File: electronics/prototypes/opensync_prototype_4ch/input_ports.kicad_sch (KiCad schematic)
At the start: 5 parts, among them J2 61611042121502, U4 SN74LVC1G17DCKR

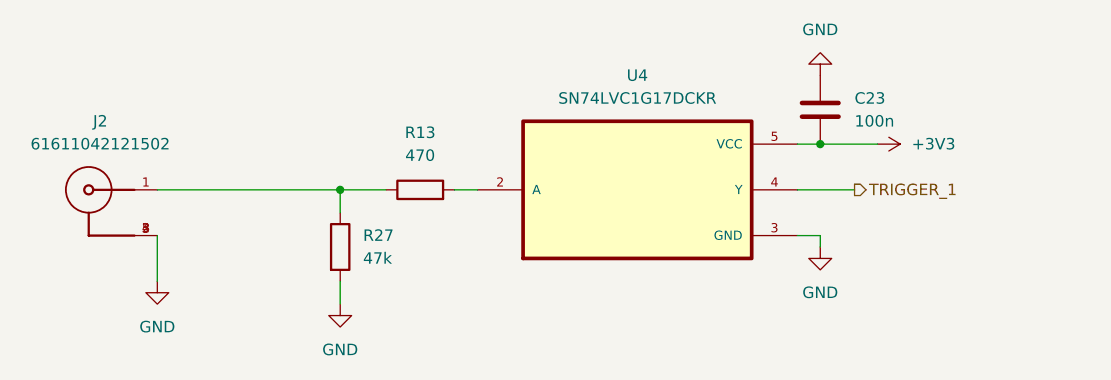
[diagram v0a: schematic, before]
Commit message: Added part numbers
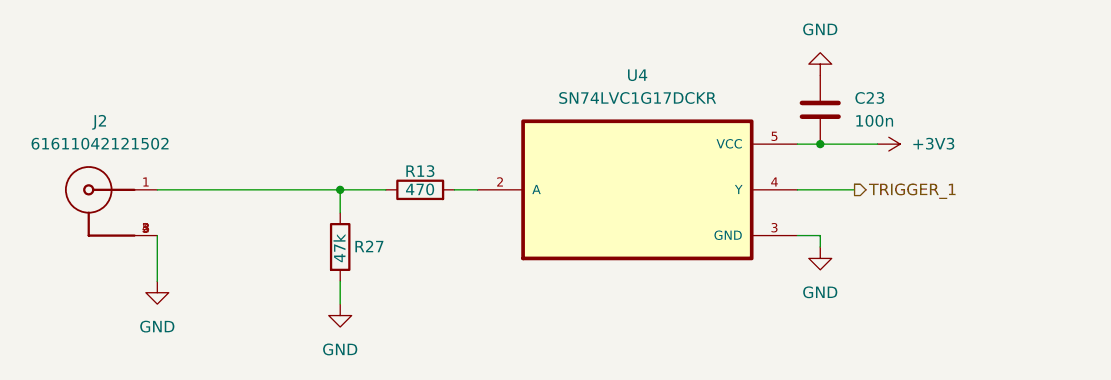
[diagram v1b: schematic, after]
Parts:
- C23: LCSC (none) -> C60474
- R13: LCSC (none) -> C482182
- R27: LCSC (none) -> C176117
- U4: LCSC (none) -> C10425
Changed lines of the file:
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@@
+			)
+		)
+		(property "LCSC" "C10425"
+			(at 138.43 66.04 0)
+			(effects
+				(font
+					(size 1.27 1.27)
+				)
+				(hide yes)
 			)
 		)
@@
 		(on_board yes)
 		(dnp no)
-		(fields_autoplaced yes)
 		(property "Reference" "R27"
-			(at 107.95 71.1199 0)
+			(at 106.934 72.39 0)
 			(effects
 				(font
@@
 		)
 		(property "Value" "47k"
-			(at 107.95 73.6599 0)
+			(at 105.41 74.168 90)
 			(effects
 				(font
@@
 			)
 		)
+		(property "LCSC" "C176117"
+			(at 105.41 72.39 0)
+			(effects
+				(font
+					(size 1.27 1.27)
+				)
+				(hide yes)
+			)
+		)
 		(pin "2"
 		)
@@
 		(on_board yes)
 		(dnp no)
-		(fields_autoplaced yes)
 		(property "Reference" "R13"
-			(at 114.3 59.69 90)
+			(at 114.3 64.008 90)
 			(effects
 				(font
@@
 		)
 		(property "Value" "470"
-			(at 114.3 62.23 90)
+			(at 114.3 66.04 90)
 			(effects
 				(font
@@
 		)
 		(property "Description" "Resistor"
+			(at 114.3 66.04 0)
+			(effects
+				(font
+					(size 1.27 1.27)
+				)
+				(hide yes)
+			)
+		)
+		(property "LCSC" "C482182"
 			(at 114.3 66.04 0)
 			(effects
@@
 			)
 		)
+		(property "LCSC" ""
+			(at 77.47 66.04 0)
+			(effects
+				(font
+					(size 1.27 1.27)
+				)
+			)
+		)
 		(pin "4"
 		)
@@
 			(at 158.75 57.15 0)
 			(effects
+				(font
+					(size 1.27 1.27)
+				)
+				(hide yes)
+			)
+		)
+		(property "LCSC" "C60474"
+			(at 158.75 57.15 0)
+			(effects

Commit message: More prototyping
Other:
- moved on the sheet: C23
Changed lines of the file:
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@@
-	)
-	(junction
-		(at 158.75 60.96)
-		(diameter 0)
-		(color 0 0 0 0)
 	)
 	(junction
@@
 		(color 0 0 0 0)
 	)
+	(junction
+		(at 171.45 60.96)
+		(diameter 0)
+		(color 0 0 0 0)
+	)
 	(wire
 		(pts
@@
 	(wire
 		(pts
-			(xy 156.21 60.96) (xy 158.75 60.96)
+			(xy 171.45 60.96) (xy 186.69 60.96)
+		)
+		(stroke
+			(width 0)
+			(type default)
+		)
+	)
+	(wire
+		(pts
+			(xy 156.21 60.96) (xy 171.45 60.96)
 		)
 		(stroke
@@
 	(wire
 		(pts
+			(xy 171.45 57.15) (xy 171.45 60.96)
+		)
+		(stroke
+			(width 0)
+			(type default)
+		)
+	)
+	(wire
+		(pts
 			(xy 110.49 66.04) (xy 105.41 66.04)
 		)
@@
 		(pts
 			(xy 105.41 66.04) (xy 105.41 68.58)
-		)
-		(stroke
-			(width 0)
-			(type default)
-		)
-	)
-	(wire
-		(pts
-			(xy 158.75 60.96) (xy 165.1 60.96)
 		)
 		(stroke
@@
 	(symbol
 		(lib_id "power:GND")
-		(at 158.75 53.34 180)
+		(at 186.69 68.58 0)
 		(unit 1)
 		(exclude_from_sim no)
@@
 		(fields_autoplaced yes)
 		(property "Reference" "#PWR014"
-			(at 158.75 46.99 0)
+			(at 186.69 74.93 0)
 			(effects
 				(font
@@
 		)
 		(property "Value" "GND"
-			(at 158.75 48.26 0)
+			(at 186.69 73.66 0)
 			(effects
 				(font
@@
 		)
 		(property "Footprint" ""
-			(at 158.75 53.34 0)
+			(at 186.69 68.58 0)
 			(effects
 				(font
@@
 		)
 		(property "Datasheet" ""
-			(at 158.75 53.34 0)
+			(at 186.69 68.58 0)
 			(effects
 				(font
@@
 		)
 		(property "Description" "Power symbol creates a global label with name \"GND\" , ground"
-			(at 158.75 53.34 0)
+			(at 186.69 68.58 0)
 			(effects
 				(font
@@
 	(symbol
 		(lib_id "power:+3V3")
-		(at 165.1 60.96 270)
+		(at 171.45 57.15 0)
 		(unit 1)
 		(exclude_from_sim no)
@@
 		(fields_autoplaced yes)
 		(property "Reference" "#PWR013"
-			(at 161.29 60.96 0)
+			(at 171.45 60.96 0)
 			(effects
 				(font
@@
 		)
 		(property "Value" "+3V3"
-			(at 168.91 60.9599 90)
-			(effects
-				(font
-					(size 1.27 1.27)
-				)
-				(justify left)
+			(at 171.45 52.07 0)
+			(effects
+				(font
+					(size 1.27 1.27)
+				)
 			)
 		)
 		(property "Footprint" ""
-			(at 165.1 60.96 0)
+			(at 171.45 57.15 0)
 			(effects
 				(font
@@
 		)
 		(property "Datasheet" ""
-			(at 165.1 60.96 0)
+			(at 171.45 57.15 0)
 			(effects
 				(font
@@
 		)
 		(property "Description" "Power symbol creates a global label with name \"+3V3\""
-			(at 165.1 60.96 0)
+			(at 171.45 57.15 0)
 			(effects
 				(font
@@
 	(symbol
 		(lib_id "Device:C")
-		(at 158.75 57.15 180)
+		(at 186.69 64.77 0)
 		(unit 1)
 		(exclude_from_sim no)
@@
 		(fields_autoplaced yes)
 		(property "Reference" "C23"
-			(at 162.56 55.8799 0)
+			(at 182.88 66.0401 0)
 			(effects
 				(font
@@
 		)
 		(property "Value" "100n"
-			(at 162.56 58.4199 0)
+			(at 182.88 63.5001 0)
 			(effects
 				(font
@@
 		)
 		(property "Footprint" "RP2350_80QFN_minimal:C_0402_1005Metric_small_pads"
-			(at 157.7848 53.34 0)
+			(at 187.6552 68.58 0)
 			(effects
 				(font
@@
 		)
 		(property "Datasheet" "~"
-			(at 158.75 57.15 0)
+			(at 186.69 64.77 0)
 			(effects
 				(font
@@
 		)
 		(property "Description" "Unpolarized capacitor"
-			(at 158.75 57.15 0)
+			(at 186.69 64.77 0)
 			(effects
 				(font
@@
 		)
 		(property "LCSC" "C60474"
-			(at 158.75 57.15 0)
-			(effects
-				(font
+			(at 186.69 64.77 0)
+			(effects
+				(font
